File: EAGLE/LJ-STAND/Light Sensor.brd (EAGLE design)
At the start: 119 x 119 mm, 122 parts

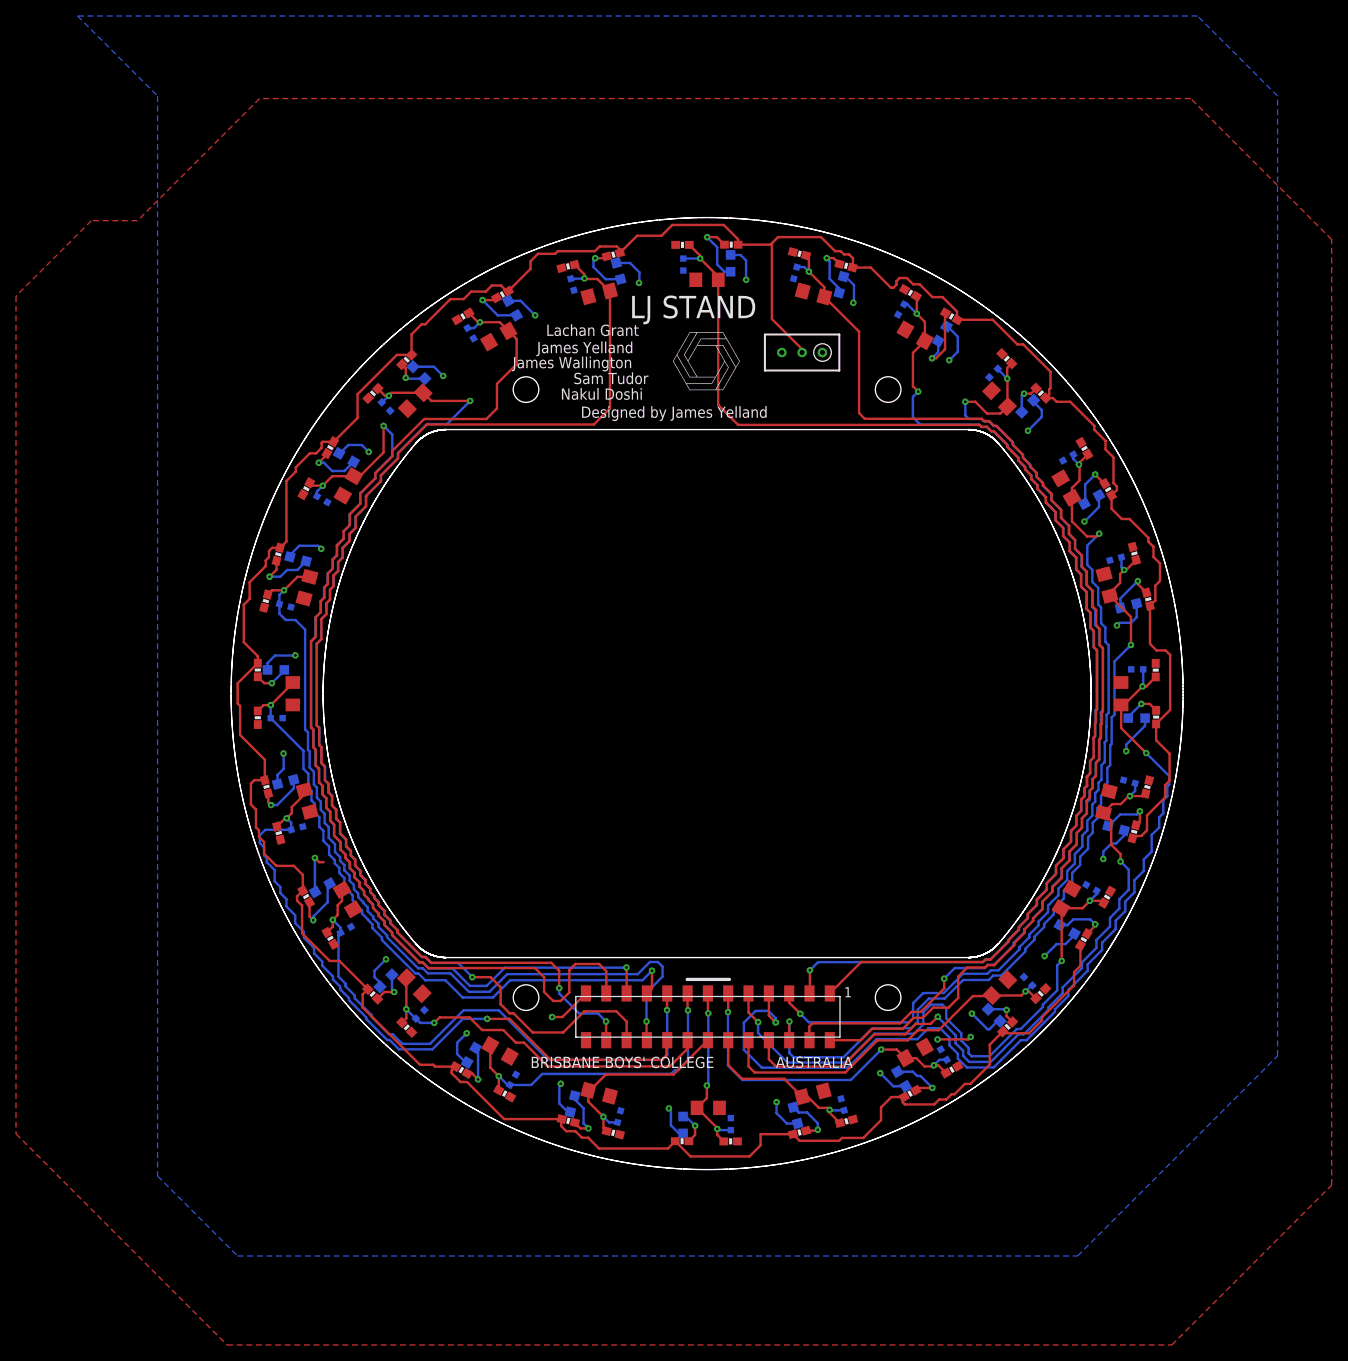
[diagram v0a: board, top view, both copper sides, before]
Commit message: changed 0805 to 0603 leds
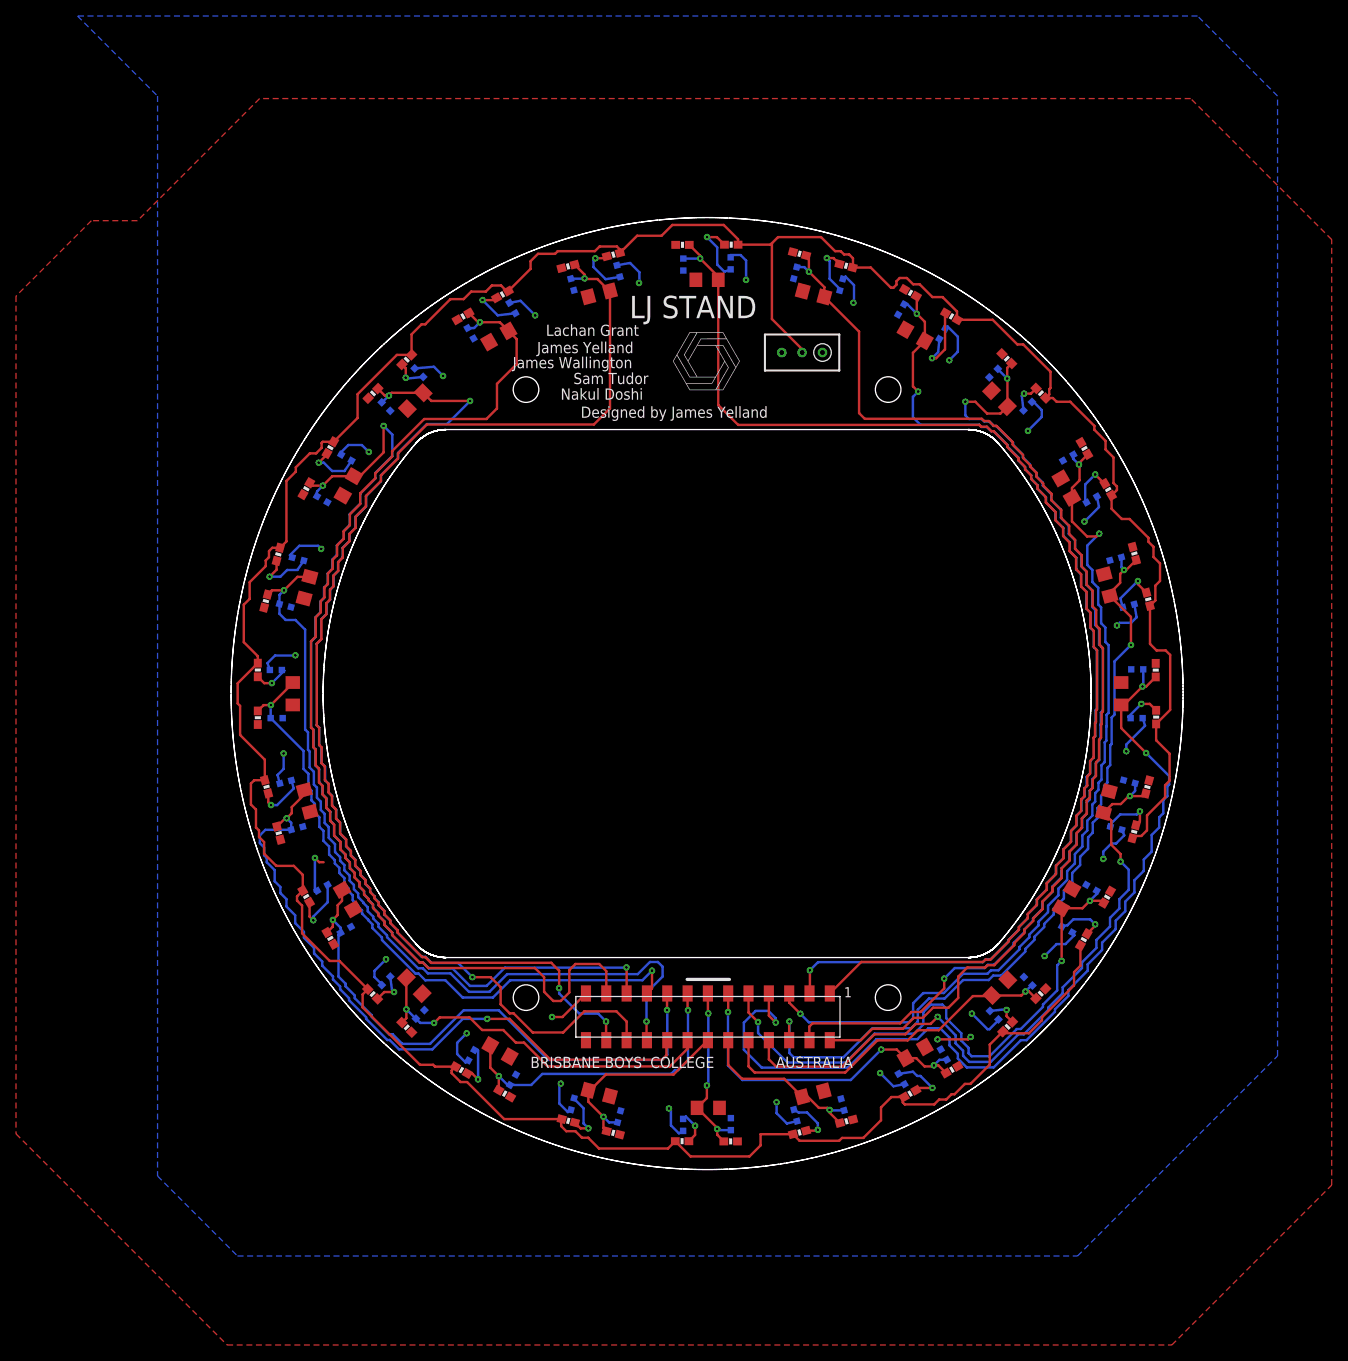
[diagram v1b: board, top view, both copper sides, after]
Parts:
- LED0, LED1, LED10, LED11, LED12, LED13, LED14, LED15, LED16, LED17, LED18, LED19, LED2, LED20, LED21, LED22, LED23, LED3, LED4, LED5, LED6, LED7, LED8, LED9: device adafruit:CHIP-LED0805 -> adafruit:CHIP-LED0603
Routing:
- net GND: track 110.3 -> 111.6 mm

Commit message: PCB fixing
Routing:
- net LED_PWR: track 416.4 -> 420.7 mm
- net N$4: track 4.01 -> 7.34 mm
- net N$22: track 4.09 -> 6.99 mm
- net N$19: track 4.60 -> 7.40 mm
- net N$10: track 3.93 -> 6.04 mm
- net N$7: track 4.83 -> 6.85 mm
- net N$14: track 6.49 -> 7.93 mm
- net N$20: track 7.58 -> 6.34 mm
- net N$17: track 7.61 -> 6.55 mm
- net LS7: track 84.5 -> 85.3 mm
- net N$23: track 6.78 -> 7.49 mm
- net N$9: track 6.32 -> 5.64 mm
- net GND: track 111.6 -> 110.9 mm
- net N$1: track 8.62 -> 8.08 mm
